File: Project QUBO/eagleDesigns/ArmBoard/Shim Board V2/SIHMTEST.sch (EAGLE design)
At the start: 11 parts, among them U1 BME280

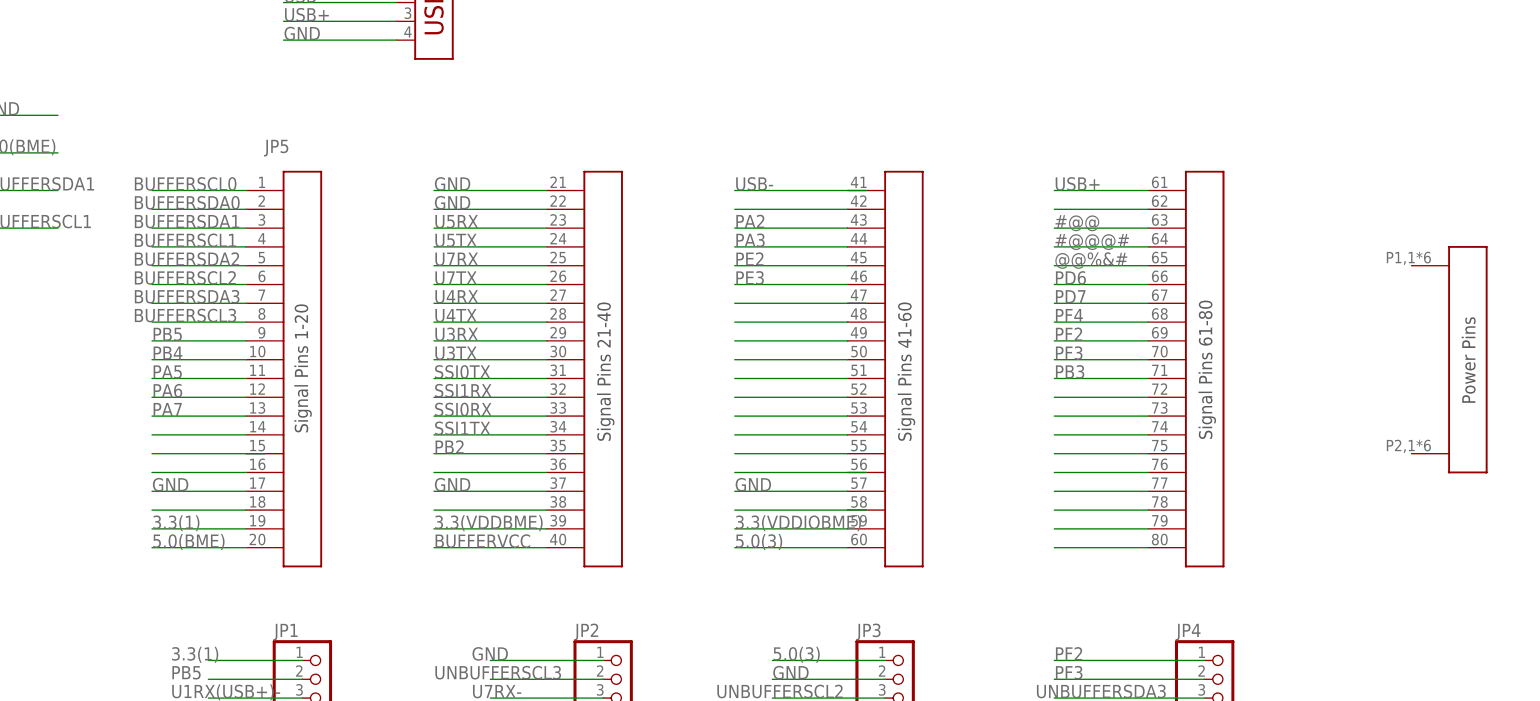
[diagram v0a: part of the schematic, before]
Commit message: 
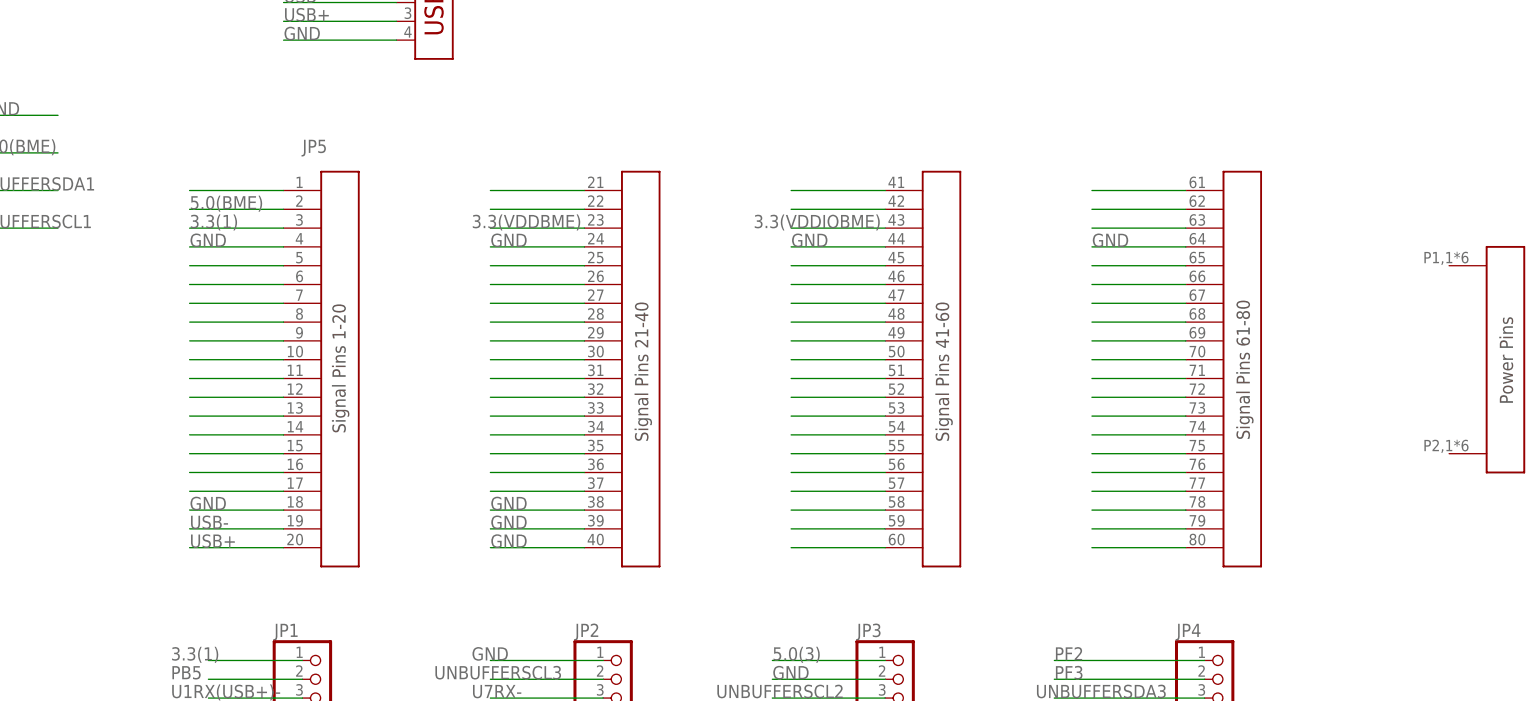
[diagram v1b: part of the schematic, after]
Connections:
- net #@@ renamed N$63
- net @@%&# renamed N$65
- net PA5 renamed N$11
- net PA6 renamed N$12
- net PA7 renamed N$13
- net PB2 renamed N$35
- net PB3 renamed N$71
- net U3RX renamed N$29
- net U3TX renamed N$30
- net U4RX renamed N$27
- net U4TX renamed N$28
- net U7RX renamed N$25
- net U7TX renamed N$26
- removed net #@@@#: JP5.P$64
- removed net N$2: JP5.P$42
- removed net N$28 (its old number): JP5.P$18
- removed net N$29 (its old number): JP5.P$38
- removed net U5RX: JP5.P$23
- removed net U5TX: JP5.P$24
- new net N$1: JP5.P$1
- new net N$10: JP5.P$10
- new net N$15: JP5.P$15
- new net N$17: JP5.P$17
- new net N$21: JP5.P$21
- new net N$22: JP5.P$22
- new net N$31: JP5.P$31
- new net N$32: JP5.P$32
- new net N$33: JP5.P$33
- new net N$34: JP5.P$34
- new net N$37: JP5.P$37
- new net N$41: JP5.P$41
- new net N$45: JP5.P$45
- new net N$46: JP5.P$46
- new net N$47: JP5.P$47
- new net N$5: JP5.P$5
- new net N$56: JP5.P$56
- new net N$57: JP5.P$57
- new net N$58: JP5.P$58
- new net N$59: JP5.P$59
- new net N$6: JP5.P$6
- new net N$60: JP5.P$60
- new net N$61: JP5.P$61
- new net N$66: JP5.P$66
- new net N$67: JP5.P$67
- new net N$68: JP5.P$68
- new net N$69: JP5.P$69
- new net N$7: JP5.P$7
- new net N$70: JP5.P$70
- new net N$77: JP5.P$77
- new net N$8: JP5.P$8
- new net N$9: JP5.P$9
- net 3.3(1): now also JP5.P$3; no longer JP5.P$19
- net 3.3(VDDBME): now also JP5.P$23; no longer JP5.P$39
- net 3.3(VDDIOBME): now also JP5.P$43; no longer JP5.P$59
- net 5.0(3): now also JP5.P$42; no longer JP5.P$60
- net 5.0(BME): now also JP5.P$2; no longer JP5.P$20
- net BUFFERSCL0: no longer JP5.P$1
- net BUFFERSCL1: no longer JP5.P$4
- net BUFFERSCL2: no longer JP5.P$6
- net BUFFERSCL3: no longer JP5.P$8
- net BUFFERSDA0: no longer JP5.P$2
- net BUFFERSDA1: no longer JP5.P$3
- net BUFFERSDA2: no longer JP5.P$5
- net BUFFERSDA3: no longer JP5.P$7
- net BUFFERVCC: no longer JP5.P$40
- net GND: now also JP5.P$18, JP5.P$24, JP5.P$38, JP5.P$39, JP5.P$4, JP5.P$40, JP5.P$44, JP5.P$64; no longer JP5.P$17, JP5.P$21, JP5.P$22, JP5.P$37, JP5.P$57, JP5.P$77
- net PA2: no longer JP5.P$43
- net PA3: no longer JP5.P$44
- net PB4: no longer JP5.P$10
- net PB5: no longer JP5.P$9
- net PD6: no longer JP5.P$66
- net PD7: no longer JP5.P$67
- net PE2: no longer JP5.P$45
- net PE3: no longer JP5.P$46
- net PF2: no longer JP5.P$69
- net PF3: no longer JP5.P$70
- net PF4: no longer JP5.P$68
- net SSI0RX: no longer JP5.P$33
- net SSI0TX: no longer JP5.P$31
- net SSI1RX: no longer JP5.P$32
- net SSI1TX: no longer JP5.P$34
- net USB+: now also JP5.P$20; no longer JP5.P$61
- net USB-: now also JP5.P$19
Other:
- moved on the sheet: JP5

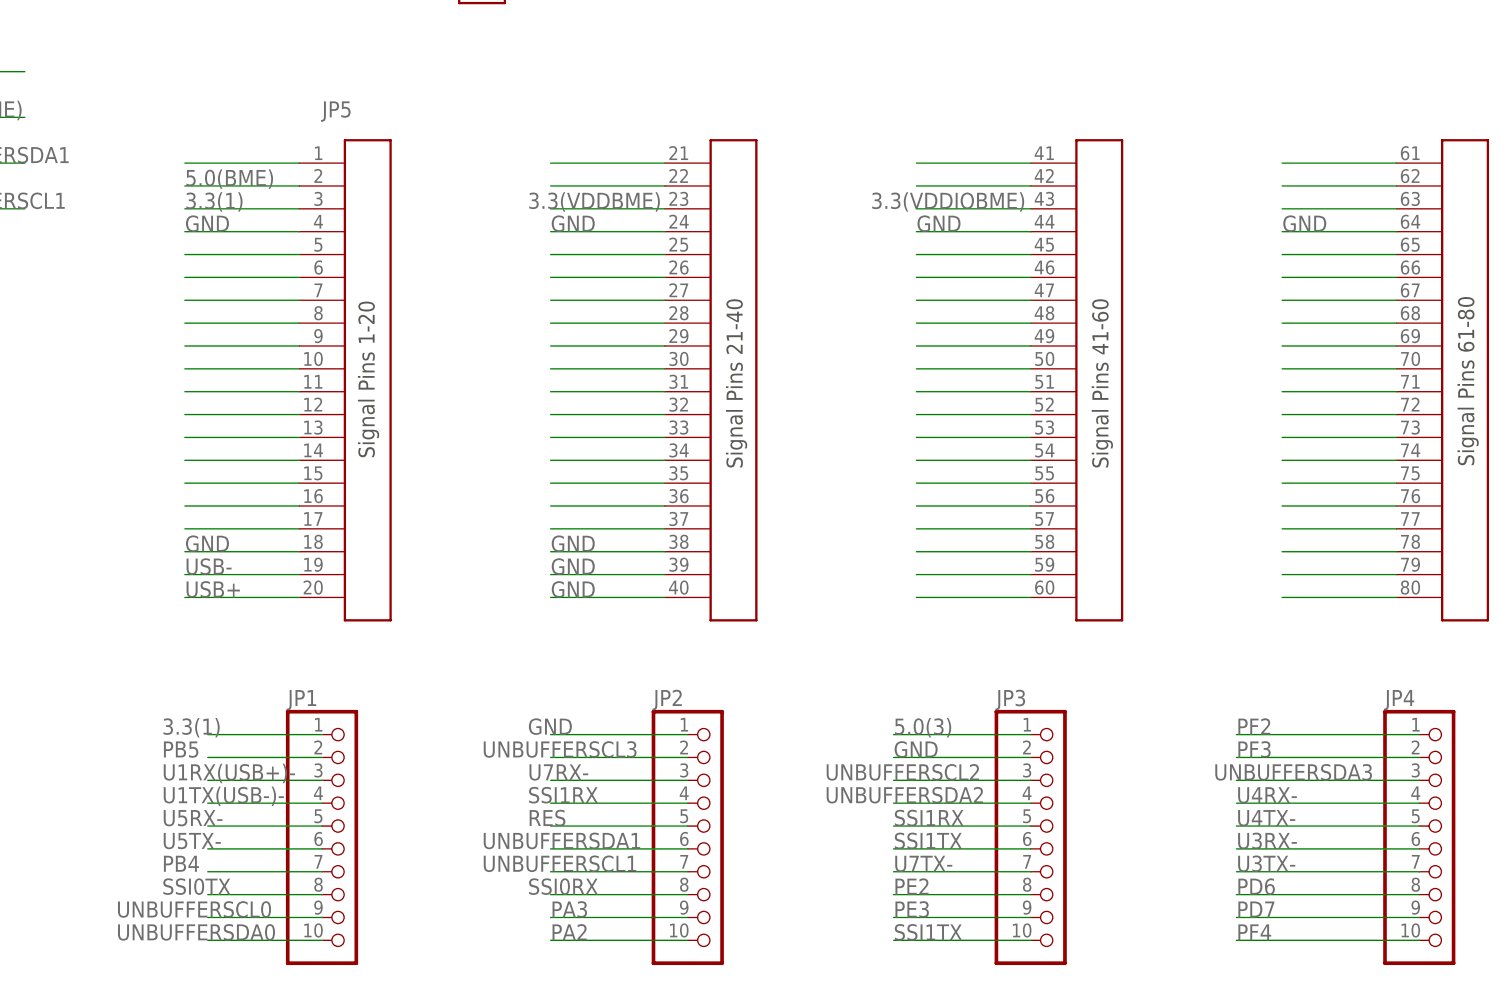
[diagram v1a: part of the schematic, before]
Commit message: 
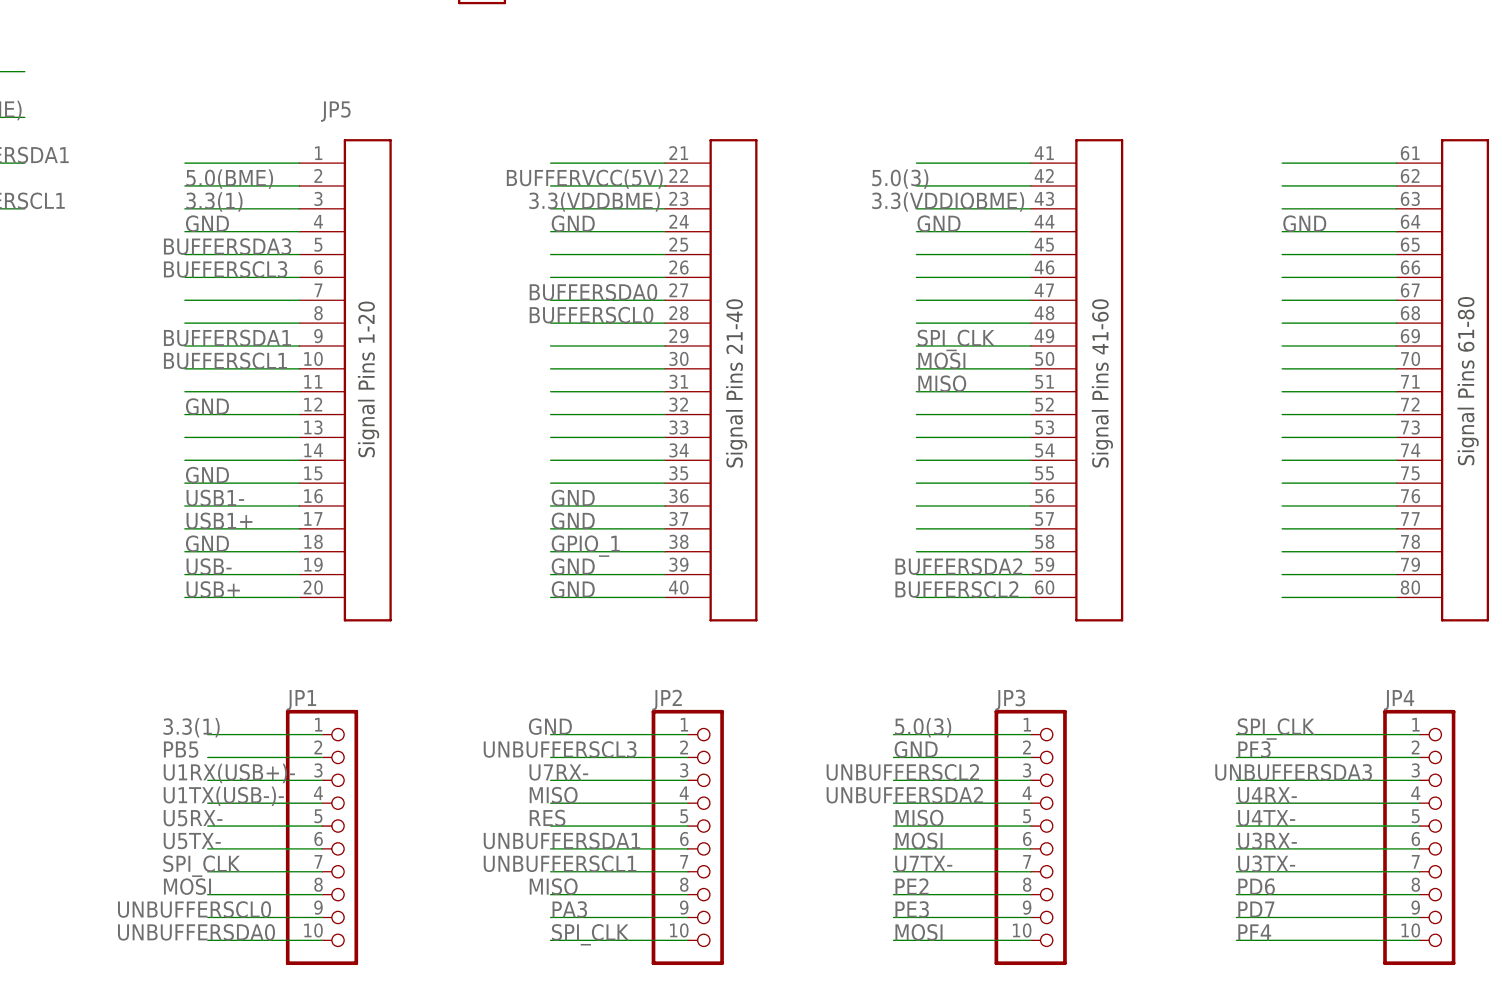
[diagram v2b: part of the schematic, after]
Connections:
- net N$16 renamed USB1-
- net N$17 renamed USB1+
- net N$22 renamed BUFFERVCC(5V)
- removed net N$10: JP5.P$10
- removed net N$12: JP5.P$12
- removed net N$15: JP5.P$15
- removed net N$27: JP5.P$27
- removed net N$28: JP5.P$28
- removed net N$36: JP5.P$36
- removed net N$37: JP5.P$37
- removed net N$49: JP5.P$49
- removed net N$5: JP5.P$5
- removed net N$50: JP5.P$50
- removed net N$51: JP5.P$51
- removed net N$59: JP5.P$59
- removed net N$6: JP5.P$6
- removed net N$60: JP5.P$60
- removed net N$9: JP5.P$9
- removed net PA2: JP2.10
- removed net PB4: JP1.7
- removed net PF2: JP4.1
- removed net SSI0RX: JP2.8
- removed net SSI0TX: JP1.8
- removed net SSI1RX: JP2.4, JP3.5
- removed net SSI1TX: JP3.10, JP3.6
- new net GPIO_1: JP5.P$38
- new net MISO: JP2.4, JP2.8, JP3.5, JP5.P$51
- new net MOSI: JP1.8, JP3.10, JP3.6, JP5.P$50
- new net SPI_CLK: JP1.7, JP2.10, JP4.1, JP5.P$49
- net BUFFERSCL0: now also JP5.P$28
- net BUFFERSCL1: now also JP5.P$10
- net BUFFERSCL2: now also JP5.P$60
- net BUFFERSCL3: now also JP5.P$6
- net BUFFERSDA0: now also JP5.P$27
- net BUFFERSDA1: now also JP5.P$9
- net BUFFERSDA2: now also JP5.P$59
- net BUFFERSDA3: now also JP5.P$5
- net GND: now also JP5.P$12, JP5.P$15, JP5.P$36, JP5.P$37; no longer JP5.P$38

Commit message: 
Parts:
- added IC1: MCP2551/SN, microchip-dspic:MCP2551/SN
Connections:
- removed net N$25: JP5.P$25
- removed net N$26: JP5.P$26
- new net CANH: IC1.CANH, JP5.P$25
- new net CANL: IC1.CANL, JP5.P$26
- new net VDD: IC1.VDD
- net GND: now also IC1.VSS
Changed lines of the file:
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@@
 <part name="X2" library="con-amp" deviceset="USB-787616" device=""/>
 <part name="JP5" library="samtec" deviceset="MPSC-01-80" device="MPSC-RA-LC"/>
+<part name="IC1" library="microchip-dspic" deviceset="MCP2551" device="/SN"/>
 </parts>
 <sheets>
@@
 <instance part="X2" gate="G$1" x="33.02" y="175.26"/>
 <instance part="JP5" gate="G$1" x="86.36" y="129.54"/>
+<instance part="IC1" gate="X" x="81.28" y="175.26"/>
 </instances>
 <busses>
@@
 <label x="0" y="124.46" size="1.778" layer="95"/>
 </segment>
+<segment>
+<pinref part="IC1" gate="X" pin="VSS"/>
+<wire x1="68.58" y1="177.8" x2="58.42" y2="177.8" width="0.1524" layer="91"/>
+<label x="58.42" y="177.8" size="1.778" layer="95"/>
+</segment>
 </net>
 <net name="UNBUFFERSCL1" class="0">
@@
 </segment>
 </net>
-<net name="N$25" class="0">
-<segment>
-<pinref part="JP5" gate="G$1" pin="P$25"/>
-<wire x1="53.34" y1="142.24" x2="40.64" y2="142.24" width="0.1524" layer="91"/>
-</segment>
-</net>
-<net name="N$26" class="0">
-<segment>
-<pinref part="JP5" gate="G$1" pin="P$26"/>
-<wire x1="53.34" y1="139.7" x2="40.64" y2="139.7" width="0.1524" layer="91"/>
-</segment>
-</net>
 <net name="N$29" class="0">
 <segment>
@@
 </segment>
 </net>
+<net name="CANH" class="0">
+<segment>
+<pinref part="IC1" gate="X" pin="CANH"/>
+<wire x1="93.98" y1="177.8" x2="101.6" y2="177.8" width="0.1524" layer="91"/>
+<label x="96.52" y="177.8" size="1.778" layer="95"/>
+</segment>
+<segment>
+<pinref part="JP5" gate="G$1" pin="P$25"/>
+<wire x1="53.34" y1="142.24" x2="40.64" y2="142.24" width="0.1524" layer="91"/>
+<label x="40.64" y="142.24" size="1.778" layer="95"/>
+</segment>
+</net>
+<net name="CANL" class="0">
+<segment>
+<pinref part="IC1" gate="X" pin="CANL"/>
+<wire x1="93.98" y1="175.26" x2="101.6" y2="175.26" width="0.1524" layer="91"/>
+<label x="96.52" y="175.26" size="1.778" layer="95"/>
+</segment>
+<segment>
+<pinref part="JP5" gate="G$1" pin="P$26"/>
+<wire x1="53.34" y1="139.7" x2="40.64" y2="139.7" width="0.1524" layer="91"/>
+<label x="40.64" y="139.7" size="1.778" layer="95"/>
+</segment>
+</net>
+<net name="VDD" class="0">
+<segment>
+<pinref part="IC1" gate="X" pin="VDD"/>
+<wire x1="68.58" y1="175.26" x2="58.42" y2="175.26" width="0.1524" layer="91"/>
+<label x="58.42" y="175.26" size="1.778" layer="95"/>
+</segment>
+</net>

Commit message: 
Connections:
- removed net PF3: JP4.2
- new net CANRX: IC1.RXD, JP2.4
- new net CANTX: IC1.TXD, JP4.2
- net GND: now also IC1.RS
- net MISO: no longer JP2.4

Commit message: 
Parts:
- added R1, R2: (no value), resistor:R-US_0204/2V
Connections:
- removed net N$62: JP5.P$62
- new net N$2: IC1.VREF, R1.2, R2.1
- net GND: now also R2.2
- net VDD: now also JP5.P$62, R1.1
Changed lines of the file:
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@@
 <part name="JP5" library="samtec" deviceset="MPSC-01-80" device="MPSC-RA-LC"/>
 <part name="IC1" library="microchip-dspic" deviceset="MCP2551" device="/SN"/>
+<part name="R1" library="resistor" deviceset="R-US_" device="0204/2V"/>
+<part name="R2" library="resistor" deviceset="R-US_" device="0204/2V"/>
 </parts>
 <sheets>
@@
 <instance part="JP5" gate="G$1" x="86.36" y="129.54"/>
 <instance part="IC1" gate="X" x="81.28" y="175.26"/>
+<instance part="R1" gate="G$1" x="119.38" y="180.34" rot="R270"/>
+<instance part="R2" gate="G$1" x="119.38" y="165.1" rot="R270"/>
 </instances>
 <busses>
@@
 <label x="96.52" y="180.34" size="1.778" layer="95"/>
 </segment>
+<segment>
+<pinref part="R2" gate="G$1" pin="2"/>
+<wire x1="119.38" y1="160.02" x2="129.54" y2="160.02" width="0.1524" layer="91"/>
+<label x="124.46" y="160.02" size="1.778" layer="95"/>
+</segment>
 </net>
 <net name="UNBUFFERSCL1" class="0">
@@
 </segment>
 </net>
-<net name="N$62" class="0">
-<segment>
-<pinref part="JP5" gate="G$1" pin="P$62"/>
-<wire x1="134.62" y1="149.86" x2="121.92" y2="149.86" width="0.1524" layer="91"/>
-</segment>
-</net>
 <net name="N$63" class="0">
 <segment>
@@
 <label x="58.42" y="175.26" size="1.778" layer="95"/>
 </segment>
+<segment>
+<pinref part="JP5" gate="G$1" pin="P$62"/>
+<wire x1="134.62" y1="149.86" x2="121.92" y2="149.86" width="0.1524" layer="91"/>
+<label x="121.92" y="149.86" size="1.778" layer="95"/>
+</segment>
+<segment>
+<pinref part="R1" gate="G$1" pin="1"/>
+<wire x1="119.38" y1="185.42" x2="129.54" y2="185.42" width="0.1524" layer="91"/>
+<label x="124.46" y="185.42" size="1.778" layer="95"/>
+</segment>
 </net>
 <net name="CANRX" class="0">
@@
 </segment>
 </net>
+<net name="N$2" class="0">
+<segment>
+<pinref part="R1" gate="G$1" pin="2"/>
+<pinref part="R2" gate="G$1" pin="1"/>
+<wire x1="119.38" y1="175.26" x2="119.38" y2="172.72" width="0.1524" layer="91"/>
+<pinref part="IC1" gate="X" pin="VREF"/>
+<wire x1="119.38" y1="172.72" x2="119.38" y2="170.18" width="0.1524" layer="91"/>
+<wire x1="119.38" y1="172.72" x2="93.98" y2="172.72" width="0.1524" layer="91"/>
+<junction x="119.38" y="172.72"/>
+</segment>
+</net>
